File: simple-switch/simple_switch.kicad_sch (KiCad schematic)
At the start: 13 parts, among them J1 CON_HDR_100MILS_M_TH_2X8

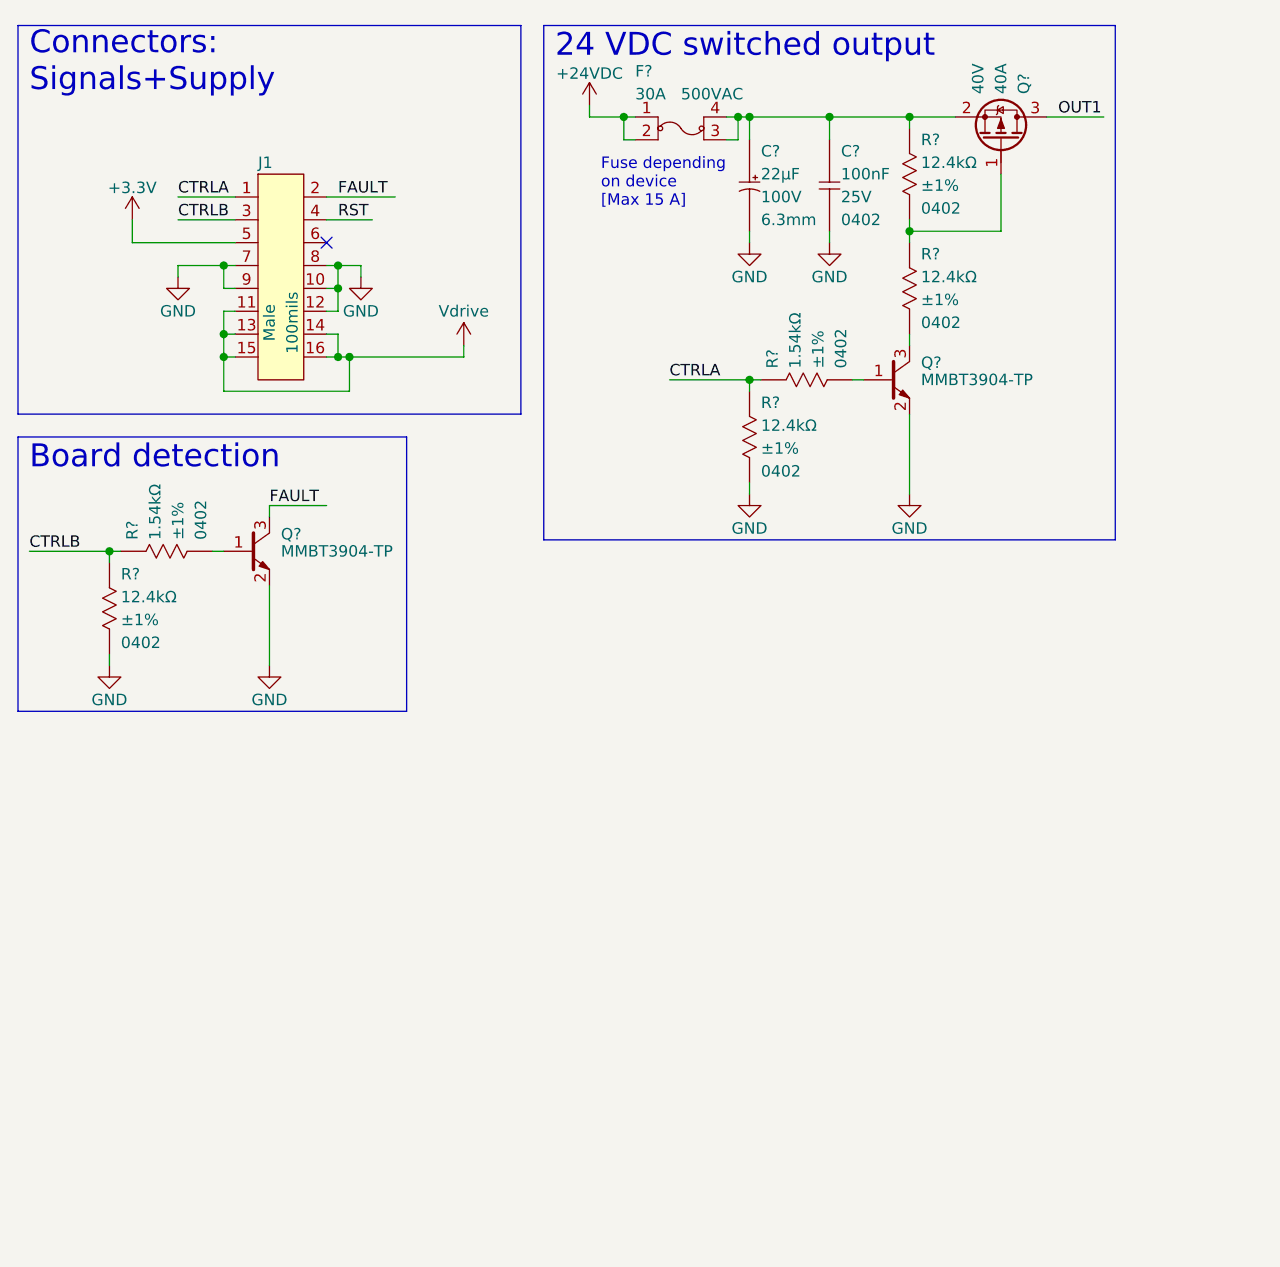
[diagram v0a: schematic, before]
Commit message: rename project, comple simple switch layout, fix thermal reliefs
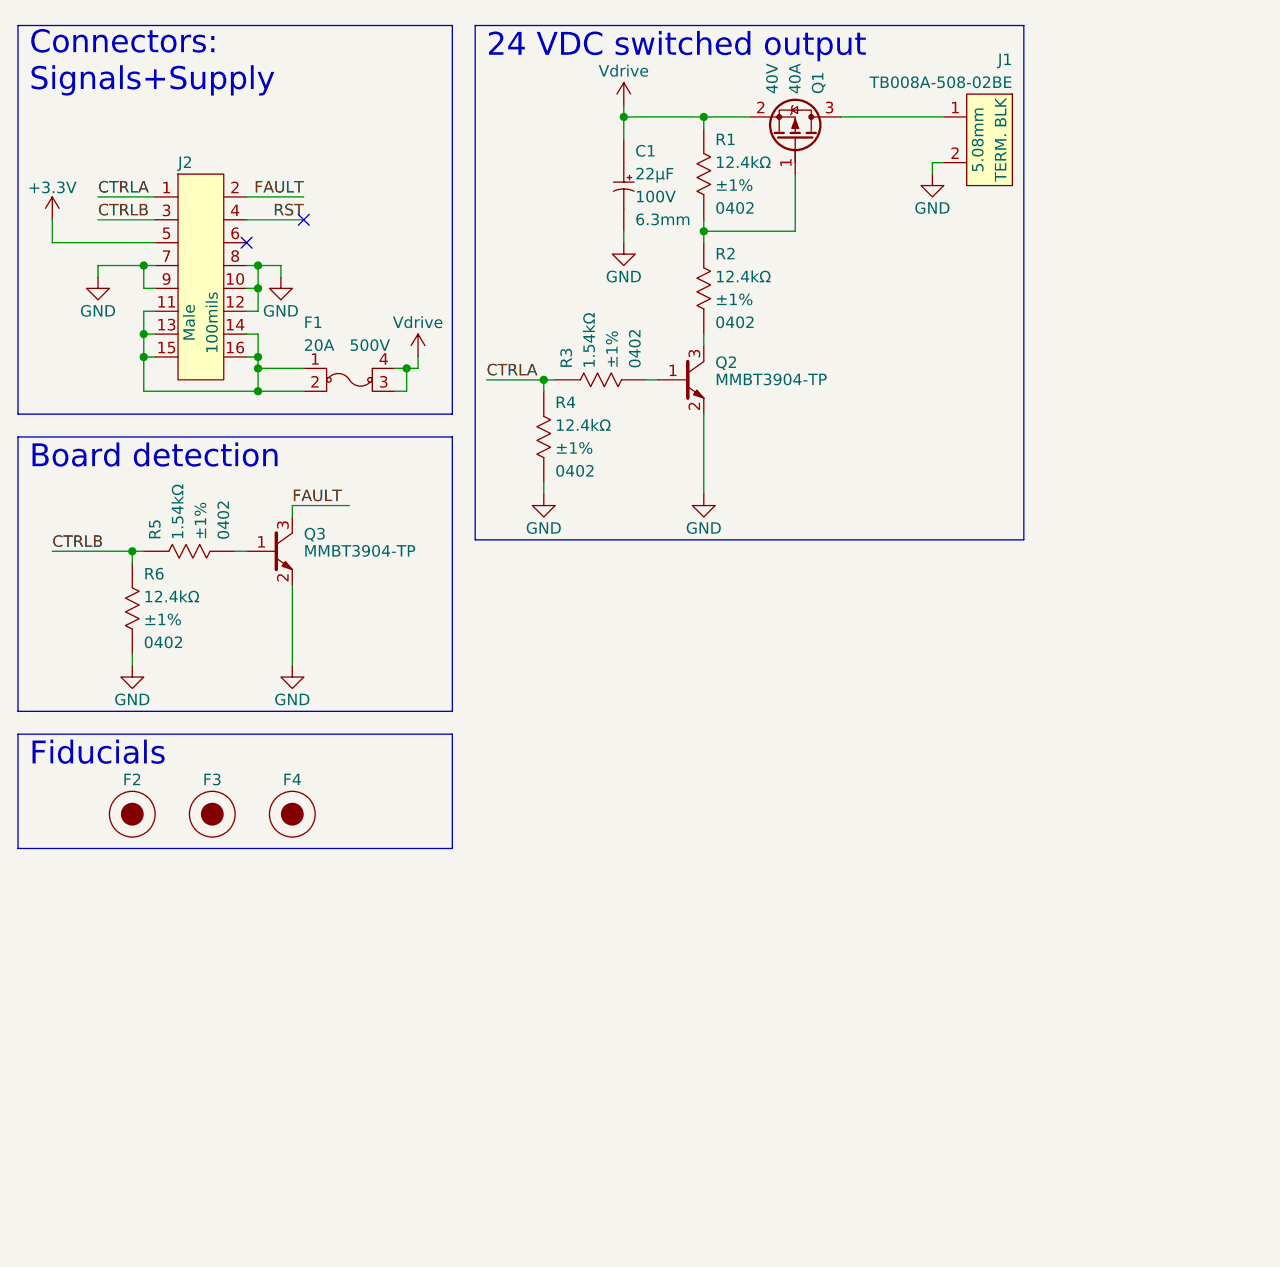
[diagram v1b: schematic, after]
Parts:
- removed C?: CAP_CER_100NF_25V_0402, connaxio-capacitors:CAP_CER_0402_1005M, symbol connaxio-capacitors:CAP_CER_100NF_25V_0402
- removed F?: FUS_BLADE_3522, connaxio-connectors:FUS_BLADE_3522, symbol connaxio-connectors:FUS_BLADE_3522
- added F1: FUS_BLADE_MINI_3588-1, connaxio-connectors:FUS_BLADE_MINI_3588-1, symbol connaxio-connectors:FUS_BLADE_MINI_3588-1
- added F2, F3, F4: FID_1X3, connaxio-mechanical:FID_1X3, symbol connaxio-mechanical:FID_1X3
- added J1: CON_TERM_BLK_1X2_TB008A-508-02BE, connaxio-connectors:CON_TERM_BLK_1X2_TB008A-508-02BE, symbol connaxio-connectors:CON_TERM_BLK_1X2_TB008A-508-02BE
- gave numbers to parts that had none: 10
- renumbered J1 to J2
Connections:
- net GND: now also J1.2
- net Vdrive: now also C1.1, Q1.2 (S), R1.1, F1.3, F1.4; no longer J2.11, J2.13, J2.14, J2.15, J2.16
- net OUT1: no longer names the net of Q1.3 (D)
- net OUT1: now also J1.1
- new net: F1.1, F1.2, J2.11, J2.13, J2.14, J2.15, J2.16
- no-connect marks 1 -> 2
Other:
- note added: "Fiducials"
- note removed: "Fuse depending on device [Max 15 A]"
- moved on the sheet: C1, J2, Q1, Q2, Q3, R1, R2, R3, R4, R5, R6

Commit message: Inverted motor controls for open-drain operation and manual switch override compatibility
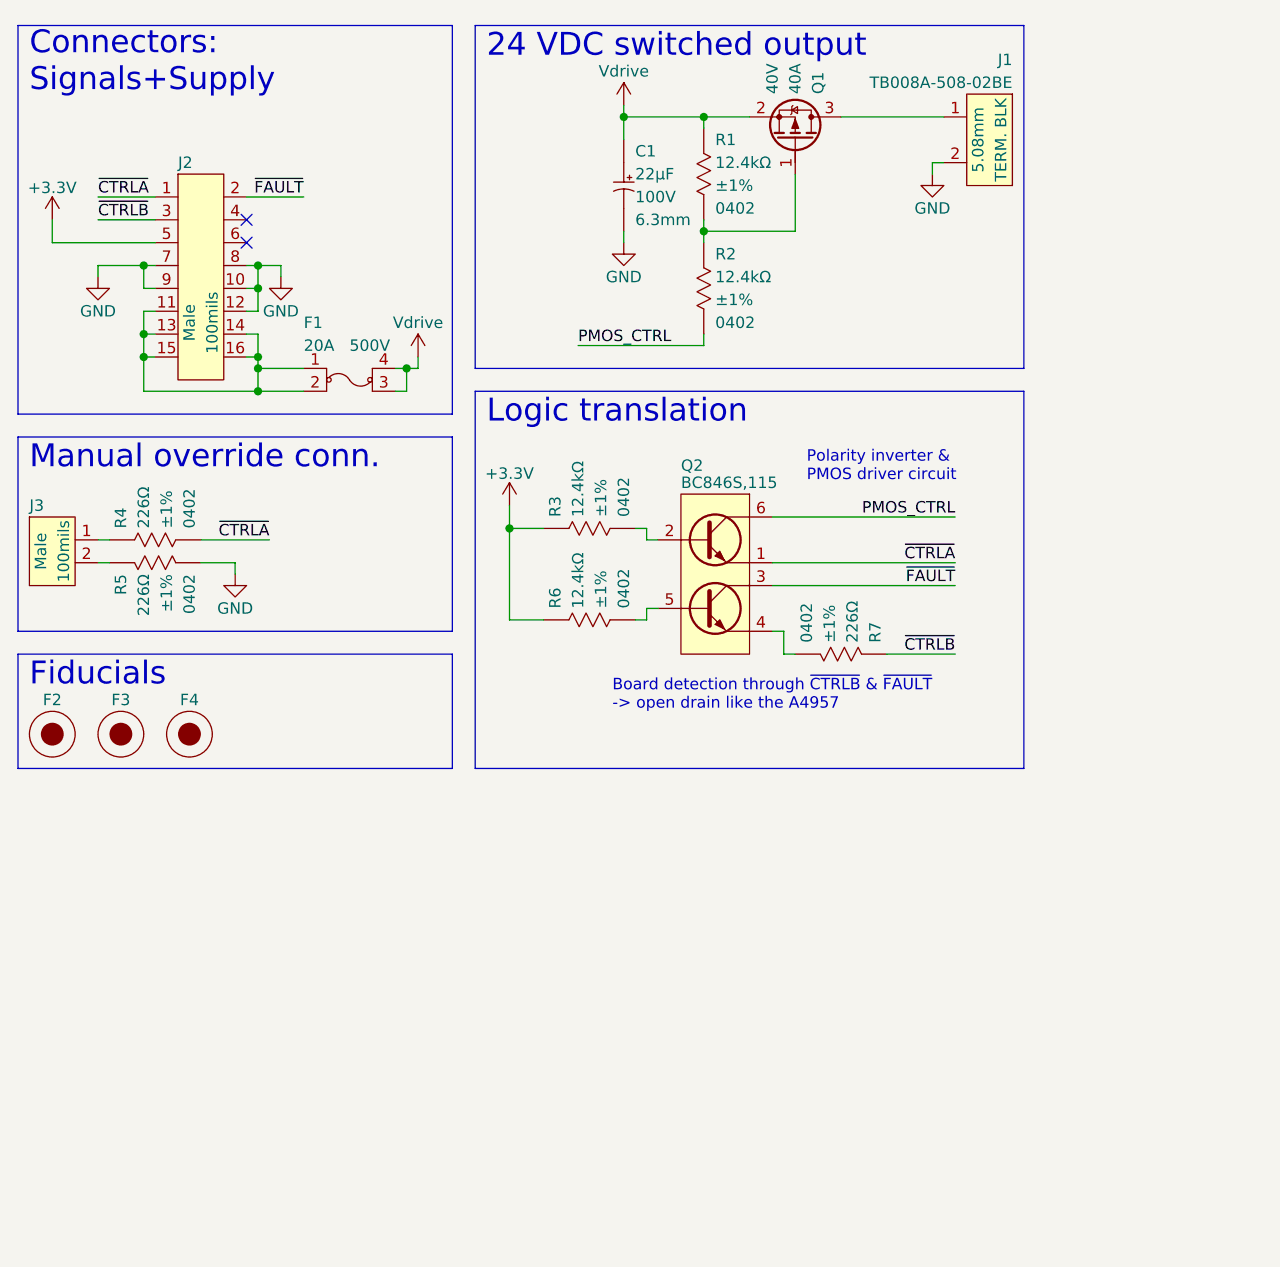
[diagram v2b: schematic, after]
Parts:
- removed Q2, Q3: TRX_NPN_MMBT3904-TP, connaxio-sop:SOT-23-3, symbol connaxio-transistors:TRX_NPN_MMBT3904-TP
- removed R3, R5: RES_1.54KΩ_1%_0402, connaxio-resistors:RES_0402_1005M, symbol connaxio-resistors:RES_1.54KΩ_1%_0402
- removed R4: RES_12.4KΩ_1%_0402, connaxio-resistors:RES_0402_1005M, symbol connaxio-resistors:RES_12.4KΩ_1%_0402
- added J3: CON_HDR_100MILS_M_TH_1X2, connaxio-connectors:CON_HDR_100MILS_M_TH_1X2, symbol connaxio-connectors:CON_HDR_100MILS_M_TH_1X2
- added Q2: TRX_2NPN_BC846S,115, connaxio-sop:SOT-363_SC-70-6, symbol connaxio-transistors:TRX_2NPN_BC846S,115
- added R3: RES_12.4KΩ_1%_0402, connaxio-resistors:RES_0402_1005M, symbol connaxio-resistors:RES_12.4KΩ_1%_0402
- added R4, R5, R7: RES_226Ω_1%_0402, connaxio-resistors:RES_0402_1005M, symbol connaxio-resistors:RES_226Ω_1%_0402
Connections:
- net +3.3V: now also R6.1, R3.1
- net GND: now also R5.2; no longer R6.2
- net PMOS_CTRL: now reaches R2.2
- net PMOS_CTRL: now also Q2.6 (C1)
- net CTRLA renamed ~{CTRLA}
- net ~{CTRLA}: now also Q2.1 (E1), R4.2
- net CTRLB renamed ~{CTRLB}
- net ~{CTRLB}: now also R7.1; no longer R6.1
- net FAULT renamed ~{FAULT}
- net ~{FAULT}: now also Q2.3 (C2)
- net RST: no longer names the net of J2.4
- new net: Q2.2 (B1), R3.2
- new net: Q2.4 (E2), R7.2
- new net: Q2.5 (B2), R6.2
- new net: J3.1, R4.1
- new net: J3.2, R5.1
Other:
- note added: "Board detection through ~{CTRLB} & ~{FAULT} -> open drain like the A4957"
- note added: "Logic translation"
- note added: "Manual override conn."
- note added: "Polarity inverter & PMOS driver circuit"
- note removed: "Board detection"
- moved on the sheet: F2, F3, F4

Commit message: Add LEDs, fix NMOS, Add logos and infos on PCBs.
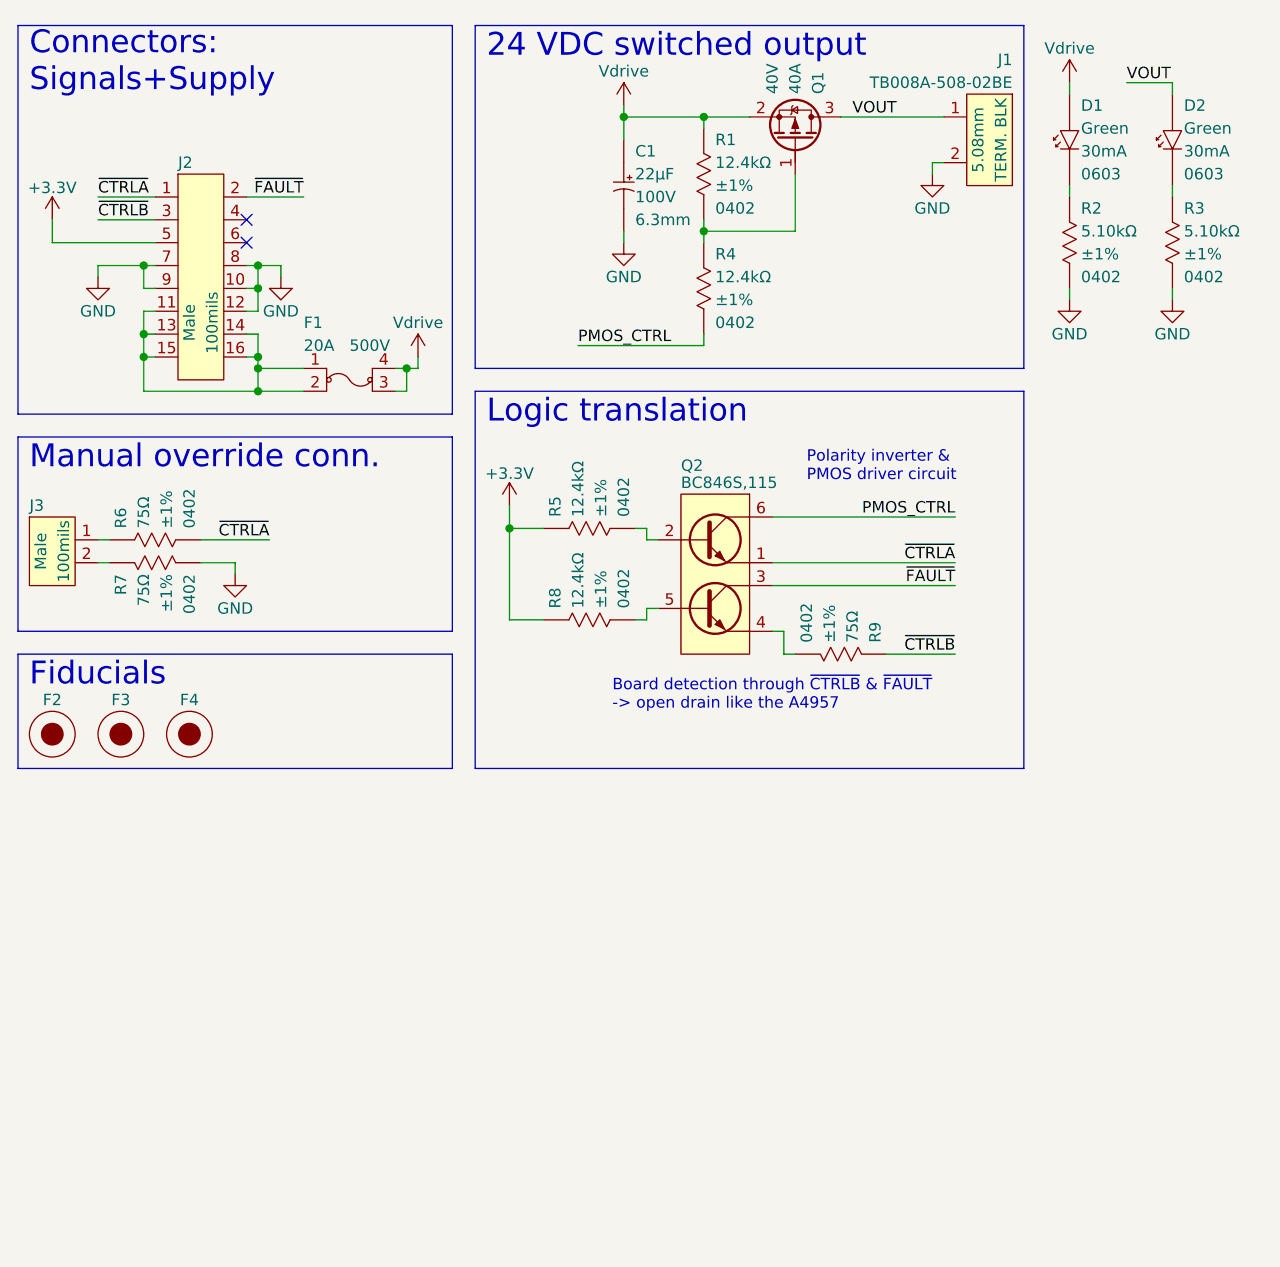
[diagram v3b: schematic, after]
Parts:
- added D1, D2: DIO_LED_GREEN_150060GS75000, connaxio-diodes:LED_0603_1608M, symbol connaxio-diodes:DIO_LED_GREEN_150060GS75000
- added R2, R3: RES_5.10KΩ_1%_0402, connaxio-resistors:RES_0402_1005M, symbol connaxio-resistors:RES_5.10KΩ_1%_0402
- R6: renamed from R4; symbol connaxio-resistors:RES_226Ω_1%_0402 -> connaxio-resistors:RES_75Ω_1%_0402; Manufacturer Part Number RMCF0402FT226R -> RMCF0402FT75R0; Property 226Ω -> 75Ω
- R7: renamed from R5; symbol connaxio-resistors:RES_226Ω_1%_0402 -> connaxio-resistors:RES_75Ω_1%_0402; Manufacturer Part Number RMCF0402FT226R -> RMCF0402FT75R0; Property 226Ω -> 75Ω
- R9: renamed from R7; symbol connaxio-resistors:RES_226Ω_1%_0402 -> connaxio-resistors:RES_75Ω_1%_0402; Manufacturer Part Number RMCF0402FT226R -> RMCF0402FT75R0; Property 226Ω -> 75Ω
- renumbered R2 to R4, R3 to R5, R6 to R8
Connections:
- net GND: now also R2.2, R3.2
- net Vdrive: now also D1.2 (A)
- net VOUT: now reaches J1.1, Q1.3 (D)
- net VOUT: now also D2.2 (A)
- new net: D1.1 (K), R2.1
- new net: D2.1 (K), R3.1
